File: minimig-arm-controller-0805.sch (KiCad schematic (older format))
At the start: 33 parts, among them CN1 USB_B_Mini, J1 Conn_01x02_Male, Q1 BC807, U1 AT91SAM7S256, U2 PIC_PIN_HEADER, X1 18.342MHz

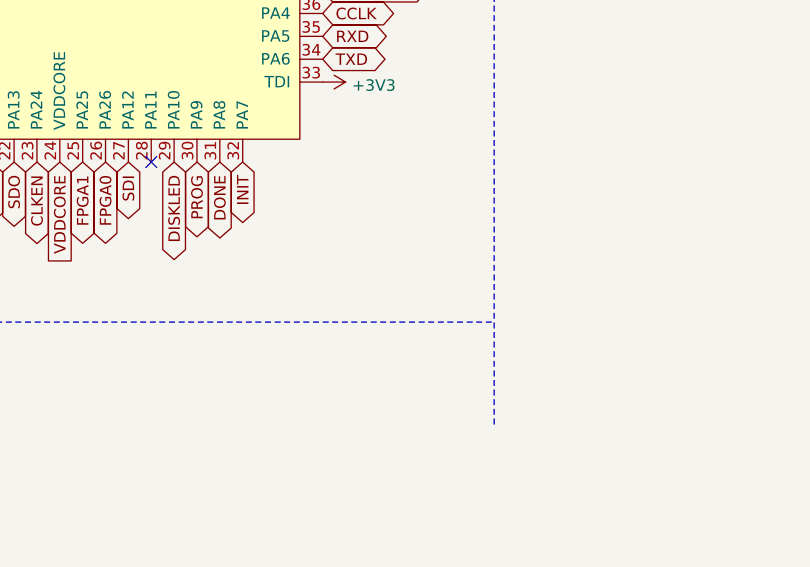
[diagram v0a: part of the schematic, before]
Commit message: add text info to schematic about TWI(I2C) pins
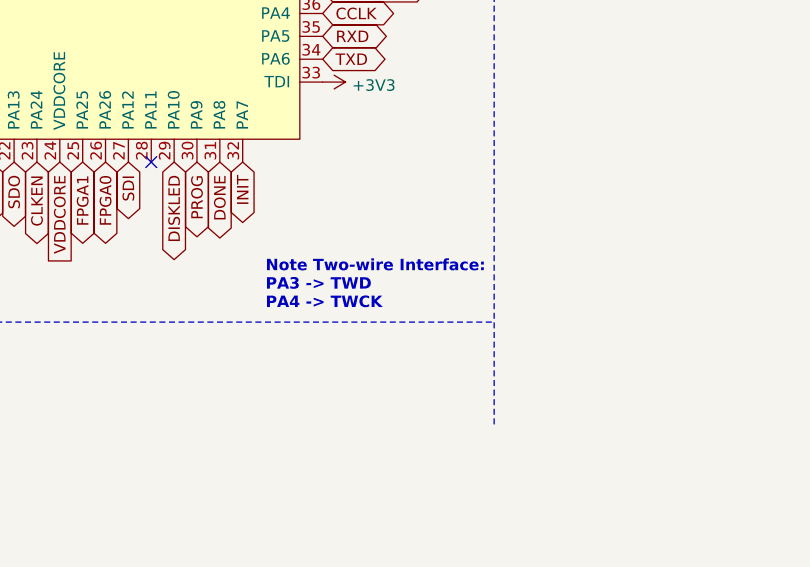
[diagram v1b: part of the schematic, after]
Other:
- note added: "Note Two-wire Interface:\nPA3 -> TWD \nPA4 -> TWCK"
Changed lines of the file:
@@
 Text Notes 1850 2400 0    50   ~ 10
 +1V8
+Text Notes 6750 5950 0    50   ~ 10
+Note Two-wire Interface:\nPA3 -> TWD \nPA4 -> TWCK
 $EndSCHEMATC

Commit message: use handsoldering footprint for HC49-SD crystal
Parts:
- X1: footprint Crystal:Crystal_SMD_HC49-SD -> Crystal:Crystal_SMD_HC49-SD_HandSoldering
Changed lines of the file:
@@
 F 0 "X1" H 5650 2050 50  0000 C CNN
 F 1 "18.342MHz" H 5800 1950 50  0000 C CNN
-F 2 "Crystal:Crystal_SMD_HC49-SD" H 5400 2000 50  0001 C CNN
+F 2 "Crystal:Crystal_SMD_HC49-SD_HandSoldering" H 5400 2000 50  0001 C CNN
 F 3 "~" H 5400 2000 50  0001 C CNN
 	1    5400 2000
